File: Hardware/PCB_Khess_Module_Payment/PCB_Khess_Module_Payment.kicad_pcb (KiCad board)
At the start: 4 copper layers, 65 x 30 mm, 22 parts, among them J3 Conn_01x08, J4 Conn_01x04, J6 Conn_01x08, U1 RASPBERRY_PI_ZERO_2_W

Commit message: fix: update PCB_Khess_Module_Payment
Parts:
- moved J3 0.30 mm to (181.7, 71.4)
- moved J6 0.30 mm to (205.6, 71.4)
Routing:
- net Column4: track 38.6 -> 33.4 mm
- net +5V_PI: track 37.5 -> 38.1 mm
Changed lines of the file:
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@@
 	(footprint "Connector_PinHeader_2.54mm:PinHeader_1x08_P2.54mm_Horizontal"
 		(layer "F.Cu")
-		(at 205.635554 71.115 -90)
+		(at 205.635554 71.415 -90)
 		(descr "Through hole angled pin header, 1x08, 2.54mm pitch, 6mm pin length, single row")
 		(tags "Through hole angled pin header THT 1x08 2.54mm single row")
@@
 	(footprint "Connector_PinHeader_2.54mm:PinHeader_1x08_P2.54mm_Horizontal"
 		(layer "F.Cu")
-		(at 181.725554 71.115 -90)
+		(at 181.725554 71.415 -90)
 		(descr "Through hole angled pin header, 1x08, 2.54mm pitch, 6mm pin length, single row")
 		(tags "Through hole angled pin header THT 1x08 2.54mm single row")
@@
 		)
 		(fp_line
-			(start -32.75 -8.38)
+			(start -32.75 -8)
 			(end -32.75 -15.25)
 			(stroke
@@
 		(fp_line
 			(start 33.75 -15.25)
-			(end 33.75 -8.38)
+			(end 33.75 -8)
 			(stroke
 				(width 0.05)
@@
 		)
 		(fp_line
-			(start 33.75 -8.38)
-			(end -32.75 -8.38)
+			(start 33.75 -8)
+			(end -32.75 -8)
 			(stroke
 				(width 0.05)
@@
 			(layer "F.CrtYd")
 		)
+		(fp_circle
+			(center -29 11.5)
+			(end -28.75 15.5)
+			(stroke
+				(width 0.05)
+				(type default)
+			)
+			(fill no)
+			(layer "F.CrtYd")
+		)
+		(fp_circle
+			(center 29 11.5)
+			(end 29 15.507805)
+			(stroke
+				(width 0.05)
+				(type default)
+			)
+			(fill no)
+			(layer "F.CrtYd")
+		)
 		(fp_line
 			(start -32.5 -12)
@@
 	)
 	(segment
-		(start 171.575 71.105554)
-		(end 171.565554 71.115)
+		(start 171.575 71.405554)
+		(end 171.565554 71.415)
 		(width 0.5)
 		(layer "F.Cu")
@@
 	(segment
 		(start 171.575 68.4)
-		(end 171.575 71.105554)
+		(end 171.575 71.405554)
 		(width 0.5)
 		(layer "F.Cu")
@@
 	)
 	(segment
+		(start 171.565554 71.415)
+		(end 171.565554 71.115)
+		(width 0.5)
+		(layer "F.Cu")
+		(net 2)
+	)
+	(segment
 		(start 159.215 49.185)
 		(end 160.37 48.03)
@@
 	)
 	(segment
-		(start 201.135 49.085)
-		(end 199.525 49.085)
+		(start 200.555554 71.415)
+		(end 200.555554 71.344446)
 		(width 0.3)
 		(layer "B.Cu")
@@
 	)
 	(segment
-		(start 202.065 69.605554)
-		(end 202.065 50.015)
+		(start 201.135 49.085)
+		(end 199.525 49.085)
 		(width 0.3)
 		(layer "B.Cu")
@@
 	)
 	(segment
-		(start 200.555554 71.115)
-		(end 202.065 69.605554)
+		(start 200.555554 71.344446)
+		(end 202.065 69.835)
+		(width 0.3)
+		(layer "B.Cu")
+		(net 9)
+	)
+	(segment
+		(start 202.065 69.835)
+		(end 202.065 50.015)
 		(width 0.3)
 		(layer "B.Cu")
@@
 	)
 	(segment
-		(start 203.095554 71.115)
-		(end 203.095554 56.279446)
+		(start 207.145 52.23)
+		(end 207.145 49.515)
 		(width 0.3)
 		(layer "B.Cu")
@@
 	)
 	(segment
-		(start 207.145 52.23)
-		(end 207.145 49.515)
+		(start 203.095554 71.415)
+		(end 203.095554 56.279446)
 		(width 0.3)
 		(layer "B.Cu")
@@
 	)
 	(segment
-		(start 181.95 64.15)
-		(end 181.3 63.5)
-		(width 0.3)
-		(layer "F.Cu")
-		(net 18)
-	)
-	(segment
-		(start 181.3 62.5)
-		(end 182.1 61.7)
+		(start 185.7 64.15)
+		(end 185.25 64.15)
 		(width 0.3)
 		(layer "F.Cu")
@@
 	)
 	(segment
-		(start 181.3 63.5)
-		(end 181.3 62.5)
+		(start 187.85 67.755)
+		(end 187.85 64.15)
 		(width 0.3)
 		(layer "F.Cu")
@@
 	)
 	(segment
-		(start 187.85 67.755)
-		(end 187.85 64.15)
+		(start 187.85 64.15)
+		(end 185.7 64.15)
 		(width 0.3)
 		(layer "F.Cu")
@@
 	)
 	(segment
-		(start 187.85 64.15)
-		(end 181.95 64.15)
+		(start 185.25 64.15)
+		(end 184.2 63.1)
 		(width 0.3)
 		(layer "F.Cu")
@@
 	)
 	(via
-		(at 182.1 61.7)
+		(at 184.2 63.1)
 		(size 0.8)
 		(drill 0.4)
@@
 	)
 	(segment
-		(start 190.1 55.2)
-		(end 183.6 61.7)
+		(start 184.2 63.1)
+		(end 184.2 61.1)
 		(width 0.3)
 		(layer "B.Cu")
@@
 	)
 	(segment
-		(start 183.6 61.7)
-		(end 182.1 61.7)
+		(start 190.1 55.2)
+		(end 184.2 61.1)
 		(width 0.3)
 		(layer "B.Cu")
@@
 	)
 	(segment
-		(start 201.01 68.120554)
-		(end 201.01 50.57)
+		(start 198.015554 71.415)
+		(end 198.015554 71.384446)
 		(width 0.3)
 		(layer "B.Cu")
@@
 	)
 	(segment
-		(start 198.015554 71.115)
-		(end 201.01 68.120554)
+		(start 198.015554 71.384446)
+		(end 201.01 68.39)
 		(width 0.3)
 		(layer "B.Cu")
@@
 	)
 	(segment
-		(start 182.175 55.425554)
-		(end 182.175 50.133004)
+		(start 201.01 68.39)
+		(end 201.01 50.57)
 		(width 0.3)
-		(layer "In2.Cu")
-		(net 23)
+		(layer "B.Cu")
+		(net 21)
 	)
 	(segment
-		(start 184.3 49.5)
-		(end 185.77 48.03)
+		(start 166.485554 71.414446)
+		(end 182.175 55.725)
 		(width 0.3)
 		(layer "In2.Cu")
@@
 	)
 	(segment
-		(start 166.485554 71.115)
-		(end 182.175 55.425554)
+		(start 182.808004 49.5)
+		(end 184.3 49.5)
 		(width 0.3)
 		(layer "In2.Cu")
@@
 	)
 	(segment
-		(start 182.808004 49.5)
-		(end 184.3 49.5)
+		(start 166.485554 71.415)
+		(end 166.485554 71.414446)
 		(width 0.3)
 		(layer "In2.Cu")
@@
 	)
 	(segment
-		(start 188.31 50.57)
-		(end 188.31 64.530554)
+		(start 182.175 55.725)
+		(end 182.175 50.133004)
+		(width 0.3)
+		(layer "In2.Cu")
+		(net 23)
+	)
+	(segment
+		(start 184.3 49.5)
+		(end 185.77 48.03)
+		(width 0.3)
+		(layer "In2.Cu")
+		(net 23)
+	)
+	(segment
+		(start 188.31 64.830554)
+		(end 181.725554 71.415)
 		(width 0.3)
 		(layer "In2.Cu")
@@
 	)
 	(segment
-		(start 188.31 64.530554)
-		(end 181.725554 71.115)
+		(start 188.31 50.57)
+		(end 188.31 64.830554)
 		(width 0.3)
 		(layer "In2.Cu")
@@
 	)
 	(segment
-		(start 175.8 69.420554)
-		(end 174.105554 71.115)
+		(start 174.105554 71.394446)
+		(end 174.105554 71.415)
 		(width 0.3)
 		(layer "F.Cu")
@@
 	(segment
 		(start 175.8 58.2)
-		(end 175.8 69.420554)
+		(end 175.8 69.7)
+		(width 0.3)
+		(layer "F.Cu")
+		(net 26)
+	)
+	(segment
+		(start 175.8 69.7)
+		(end 174.105554 71.394446)
 		(width 0.3)
 		(layer "F.Cu")
@@
 	)
 	(segment
-		(start 185.77 64.530554)
-		(end 179.185554 71.115)
+		(start 179.185554 71.314446)
+		(end 179.185554 71.415)
+		(width 0.3)
+		(layer "In2.Cu")
+		(net 27)
+	)
+	(segment
+		(start 185.77 64.73)
+		(end 179.185554 71.314446)
 		(width 0.3)
 		(layer "In2.Cu")
@@
 	(segment
 		(start 185.77 50.57)
-		(end 185.77 64.530554)
+		(end 185.77 64.73)
 		(width 0.3)
 		(layer "In2.Cu")
@@
 	)
 	(segment
-		(start 209.685 47.593004)
-		(end 209.066996 46.975)
+		(start 205.635554 71.415)
+		(end 205.635554 55.614446)
 		(width 0.3)
 		(layer "B.Cu")
@@
 	)
 	(segment
-		(start 205.635554 71.115)
-		(end 205.635554 55.614446)
+		(start 205.635554 55.614446)
+		(end 209.685 51.565)
 		(width 0.3)
 		(layer "B.Cu")
@@
 	)
 	(segment
-		(start 205.635554 55.614446)
-		(end 209.685 51.565)
+		(start 207.145 46.975)
+		(end 206.09 48.03)
 		(width 0.3)
 		(layer "B.Cu")
@@
 	)
 	(segment
-		(start 207.145 46.975)
-		(end 206.09 48.03)
+		(start 209.685 47.593004)
+		(end 209.066996 46.975)
 		(width 0.3)
 		(layer "B.Cu")
@@
 	)
 	(segment
-		(start 176.645554 71.115)
-		(end 183.23 64.530554)
+		(start 183.23 64.87)
+		(end 183.23 50.57)
+		(width 0.3)
+		(layer "In2.Cu")
+		(net 32)
+	)
+	(segment
+		(start 176.685 71.415)
+		(end 183.23 64.87)
 		(width 0.3)
 		(layer "In2.Cu")
@@
 	)
 	(segment
-		(start 183.23 64.530554)
-		(end 183.23 50.57)
+		(start 176.645554 71.415)
+		(end 176.685 71.415)
 		(width 0.3)
 		(layer "In2.Cu")
@@
 	)
 	(segment
-		(start 192.935554 71.115)
-		(end 192.935554 68.785554)
+		(start 192.935554 68.785554)
+		(end 192.925 68.775)
 		(width 0.3)
 		(layer "F.Cu")
@@
 	)
 	(segment
-		(start 192.935554 68.785554)
-		(end 192.925 68.775)
+		(start 192.935554 71.415)
+		(end 192.935554 68.785554)
 		(width 0.3)
 		(layer "F.Cu")
@@
 	)
 	(segment
-		(start 195.475554 68.800554)
-		(end 195.45 68.775)
+		(start 195.475554 71.415)
+		(end 195.475554 68.800554)
 		(width 0.3)
 		(layer "F.Cu")
@@
 	)
 	(segment
-		(start 195.475554 71.115)
-		(end 195.475554 68.800554)
+		(start 195.475554 68.800554)
+		(end 195.45 68.775)
 		(width 0.3)
 		(layer "F.Cu")
@@
 	)
 	(segment
-		(start 190.395554 71.115)
-		(end 190.395554 68.779446)
+		(start 190.395554 68.779446)
+		(end 190.4 68.775)
 		(width 0.3)
 		(layer "F.Cu")
@@
 	)
 	(segment
-		(start 190.395554 68.779446)
-		(end 190.4 68.775)
+		(start 190.395554 71.415)
+		(end 190.395554 68.779446)
 		(width 0.3)
 		(layer "F.Cu")
@@
 	)
 	(segment
-		(start 187.855554 71.115)
+		(start 187.855554 71.415)
 		(end 187.855554 68.780554)
 		(width 0.3)

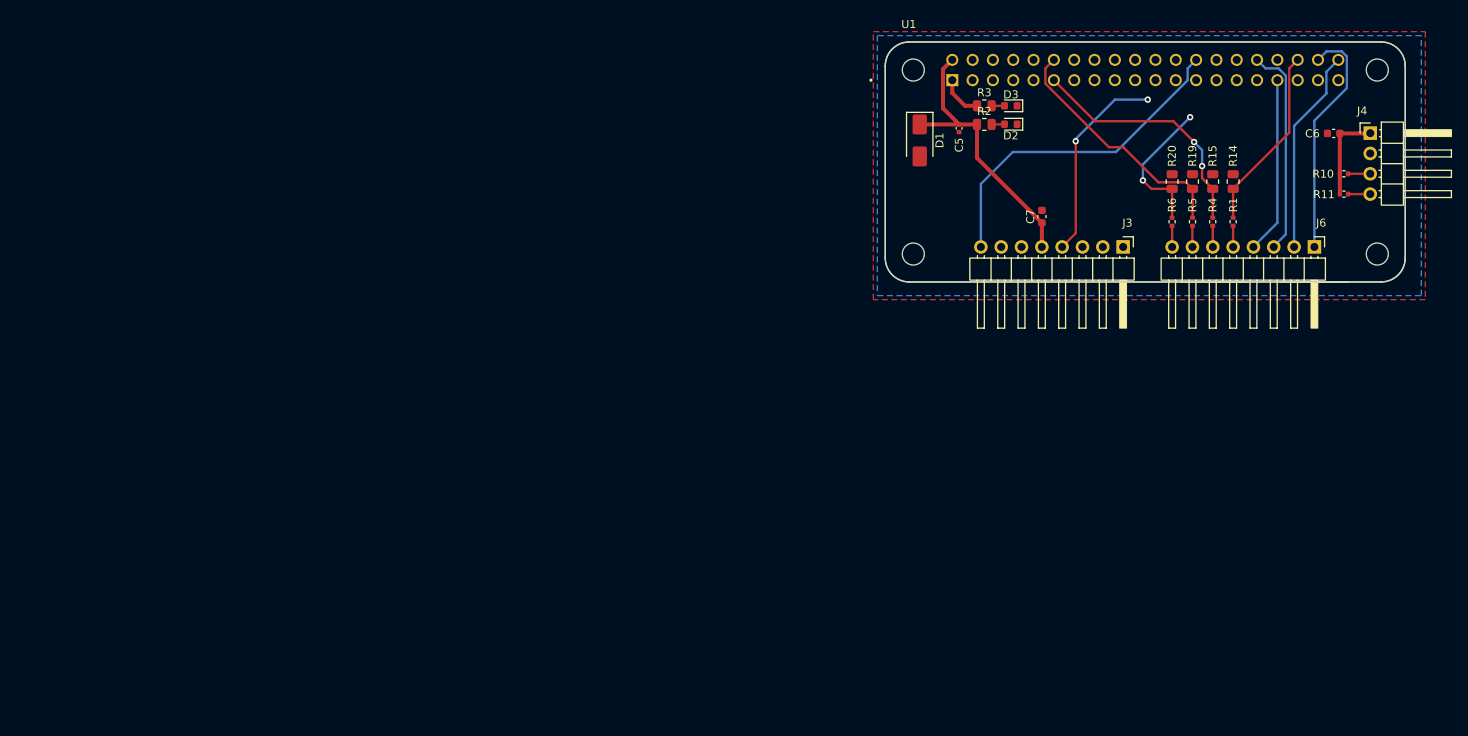
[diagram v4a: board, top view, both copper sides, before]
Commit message: fix: update two pcb and add gnd via
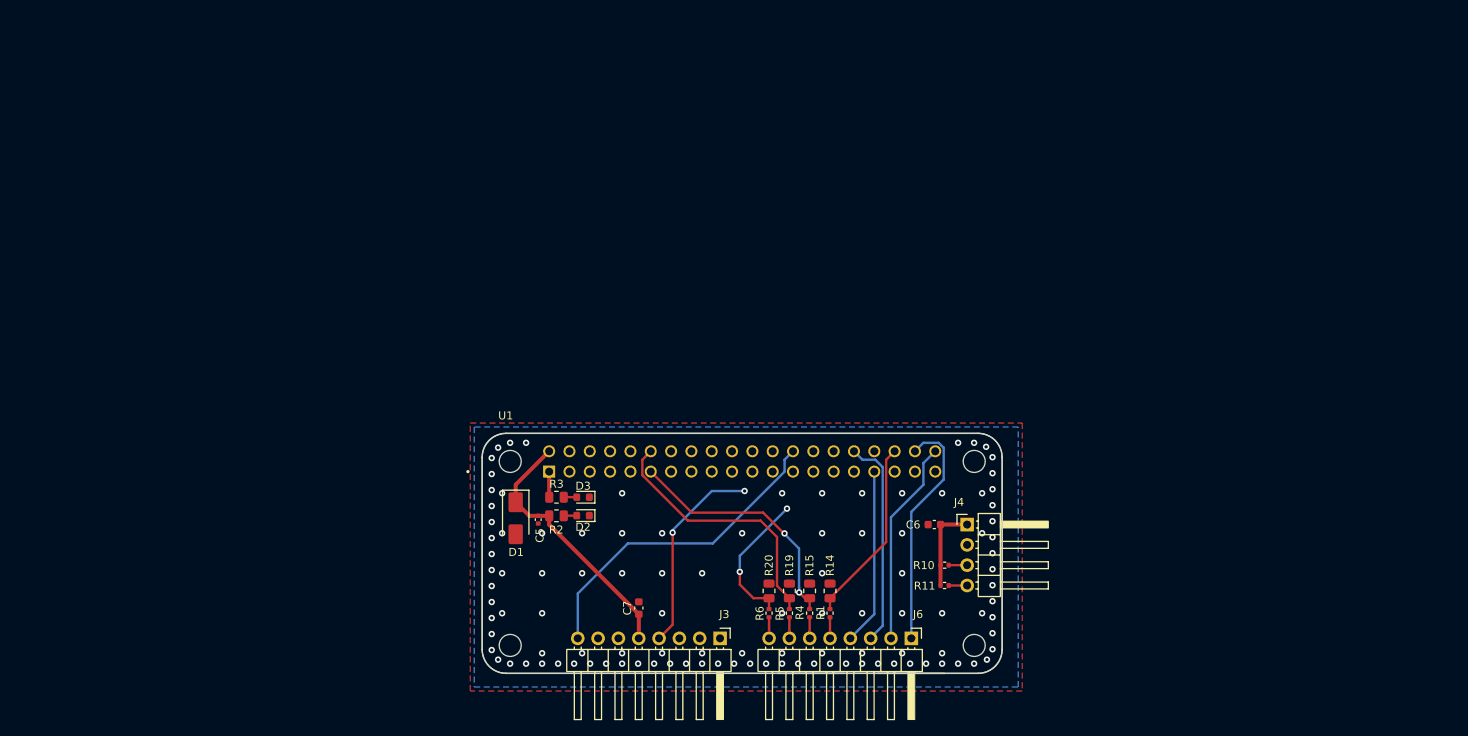
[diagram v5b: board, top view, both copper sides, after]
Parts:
- moved R2 72.5 mm to (110.9, 105.0)
- moved R3 72.5 mm to (110.9, 102.7)
- moved D3 72.5 mm to (114.2, 102.7)
- moved D2 72.5 mm to (114.2, 105.0)
- moved C5 71.8 mm to (108.6, 105.5)
- moved R15 71.8 mm to (142.5, 114.4)
- moved R19 71.8 mm to (140.0, 114.4)
- moved R14 71.8 mm to (145.1, 114.4)
- moved R20 71.8 mm to (137.5, 114.4)
- moved J4 70.2 mm to (162.2, 106.1)
- moved J6 70.2 mm to (155.2, 120.3)
- moved R4 70.2 mm to (142.5, 117.2)
- moved R5 70.2 mm to (140.0, 117.2)
- moved C7 70.2 mm to (121.2, 116.5)
- moved J3 70.2 mm to (131.3, 120.3)
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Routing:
- net IRQ: track 32.2 -> 38.6 mm
- net +3.3V_PI: track 72.7 -> 70.1 mm
- net +5V_PI: track 38.1 -> 35.8 mm
- net Column3: track 30.8 -> 33.1 mm
- net RSTO: track 41.8 -> 40.4 mm
- net GND: vias 0 -> 110

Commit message: fix: pcb
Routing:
- net SS: track 32.3 -> 29.3 mm, vias 2 -> 1
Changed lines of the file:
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@@
 	)
 	(segment
-		(start 123.718054 120.319446)
-		(end 123.718054 120.34)
-		(width 0.3)
-		(layer "F.Cu")
-		(net 26)
-	)
-	(segment
-		(start 125.4125 107.125)
-		(end 125.4125 118.625)
+		(start 129.75 107)
+		(end 125.4125 111.3375)
 		(width 0.3)
 		(layer "F.Cu")
@@
 		(net 26)
 	)
-	(via
-		(at 134.4125 101.925)
-		(size 0.8)
-		(drill 0.4)
-		(layers "F.Cu" "B.Cu")
+	(segment
+		(start 123.718054 120.319446)
+		(end 123.718054 120.34)
+		(width 0.3)
+		(layer "F.Cu")
+		(net 26)
+	)
+	(segment
+		(start 125.4125 111.3375)
+		(end 125.4125 118.625)
+		(width 0.3)
+		(layer "F.Cu")
 		(net 26)
 	)
 	(via
-		(at 125.4125 107.125)
+		(at 129.75 107)
 		(size 0.8)
 		(drill 0.4)
@@
 	)
 	(segment
-		(start 130.3125 101.925)
-		(end 125.4125 106.825)
+		(start 134.874496 101.925)
+		(end 136.8675 99.931996)
 		(width 0.3)
 		(layer "B.Cu")
@@
 	)
 	(segment
-		(start 134.4125 101.925)
-		(end 130.3125 101.925)
+		(start 134.825 101.925)
+		(end 134.874496 101.925)
 		(width 0.3)
 		(layer "B.Cu")
@@
 	)
 	(segment
-		(start 125.4125 106.825)
-		(end 125.4125 107.125)
+		(start 136.8675 98.01)
+		(end 137.9225 96.955)
 		(width 0.3)
 		(layer "B.Cu")
@@
 	)
 	(segment
-		(start 136.4375 100.988631)
-		(end 135.501131 101.925)
+		(start 136.8675 99.931996)
+		(end 136.8675 98.01)
 		(width 0.3)
-		(layer "In1.Cu")
+		(layer "B.Cu")
 		(net 26)
 	)
 	(segment
-		(start 137.9225 96.955)
-		(end 136.4375 98.44)
+		(start 129.75 107)
+		(end 134.825 101.925)
 		(width 0.3)
-		(layer "In1.Cu")
+		(layer "B.Cu")
 		(net 26)
 	)
-	(segment
-		(start 136.4375 98.44)
-		(end 136.4375 100.988631)
-		(width 0.3)
-		(layer "In1.Cu")
-		(net 26)
-	)
-	(segment
-		(start 135.501131 101.925)
-		(end 134.4125 101.925)
-		(width 0.3)
-		(layer "In1.Cu")
-		(net 26)
-	)

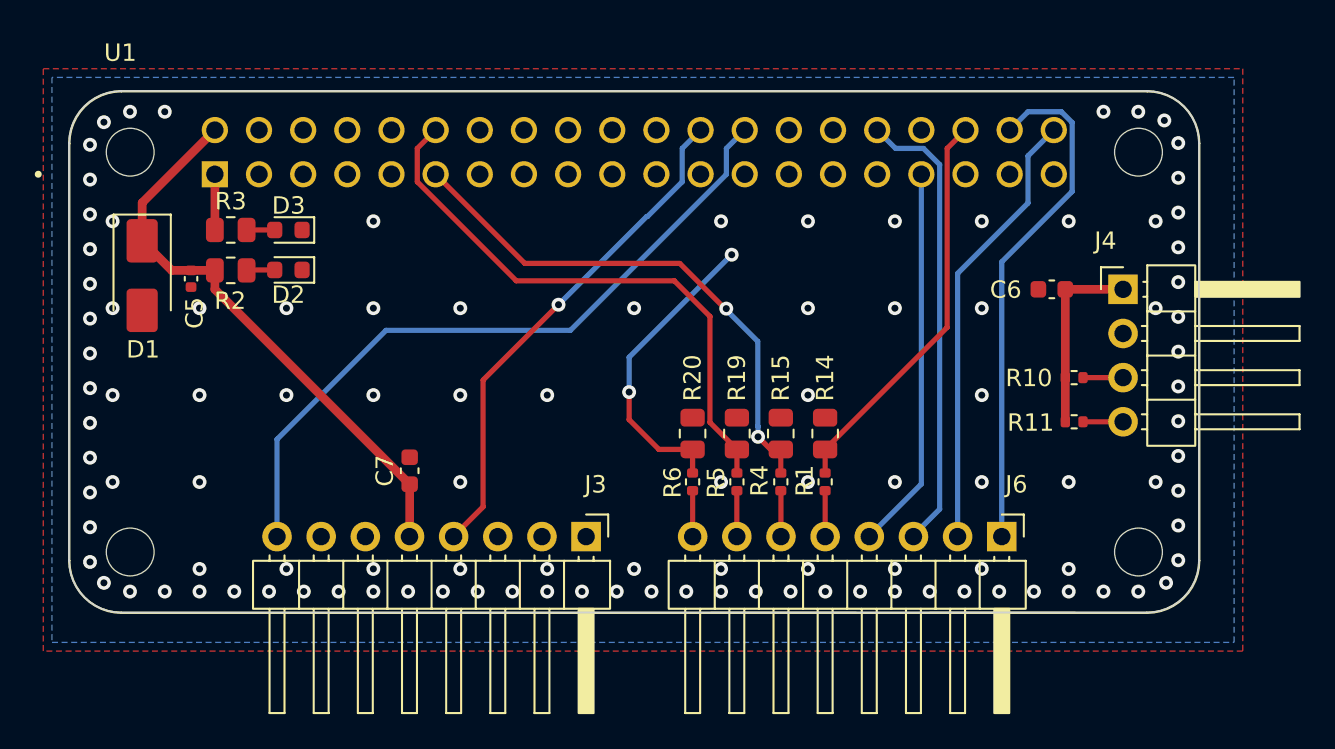
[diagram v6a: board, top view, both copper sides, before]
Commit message: fix: add gnd to all plan
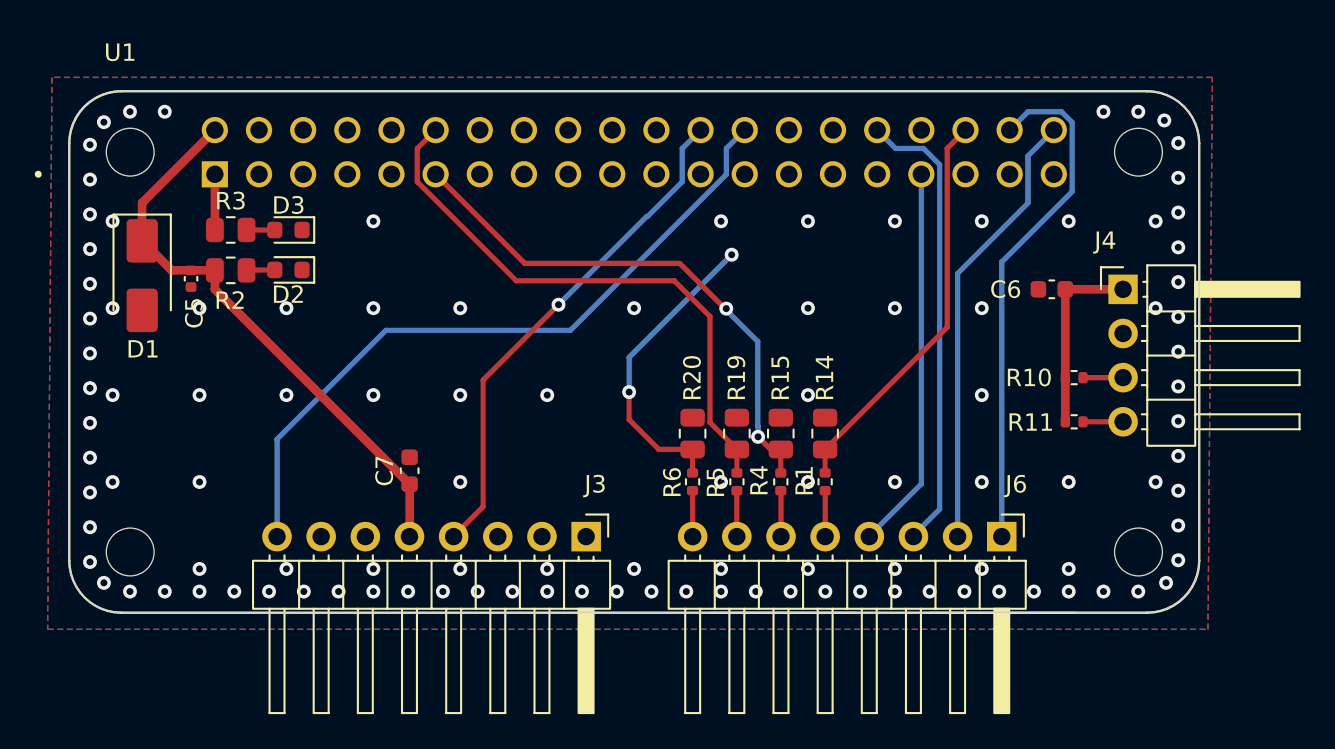
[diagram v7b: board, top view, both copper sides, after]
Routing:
- added copper zone on In1.Cu, net GND
- added copper zone on In2.Cu, net GND
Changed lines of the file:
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@@
 		(net 1)
 		(net_name "GND")
-		(layer "F.Cu")
-		(hatch edge 0.5)
-		(priority 1)
-		(connect_pads
-			(clearance 0.5)
-		)
-		(min_thickness 0.25)
-		(filled_areas_thickness no)
-		(fill yes
-			(thermal_gap 0.5)
-			(thermal_bridge_width 0.5)
-		)
-		(polygon
-			(pts
-				(xy 100.1125 93.425) (xy 169.1125 93.425) (xy 169.1125 126.925) (xy 100.1125 126.925)
-			)
-		)
-	)
-	(zone
-		(net 1)
-		(net_name "GND")
-		(layer "B.Cu")
+		(layers "F.Cu" "B.Cu" "In1.Cu" "In2.Cu")
 		(hatch edge 0.5)
 		(connect_pads
@@
 		(polygon
 			(pts
-				(xy 100.6125 93.925) (xy 100.6125 126.425) (xy 168.6125 126.425) (xy 168.6125 93.925)
+				(xy 100.6125 93.925) (xy 100.3625 125.675) (xy 167.1125 125.675) (xy 167.3625 93.925)
 			)
 		)
